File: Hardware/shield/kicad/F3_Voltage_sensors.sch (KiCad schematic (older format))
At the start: 14 parts, among them U301 LMV358, U401 LMV358

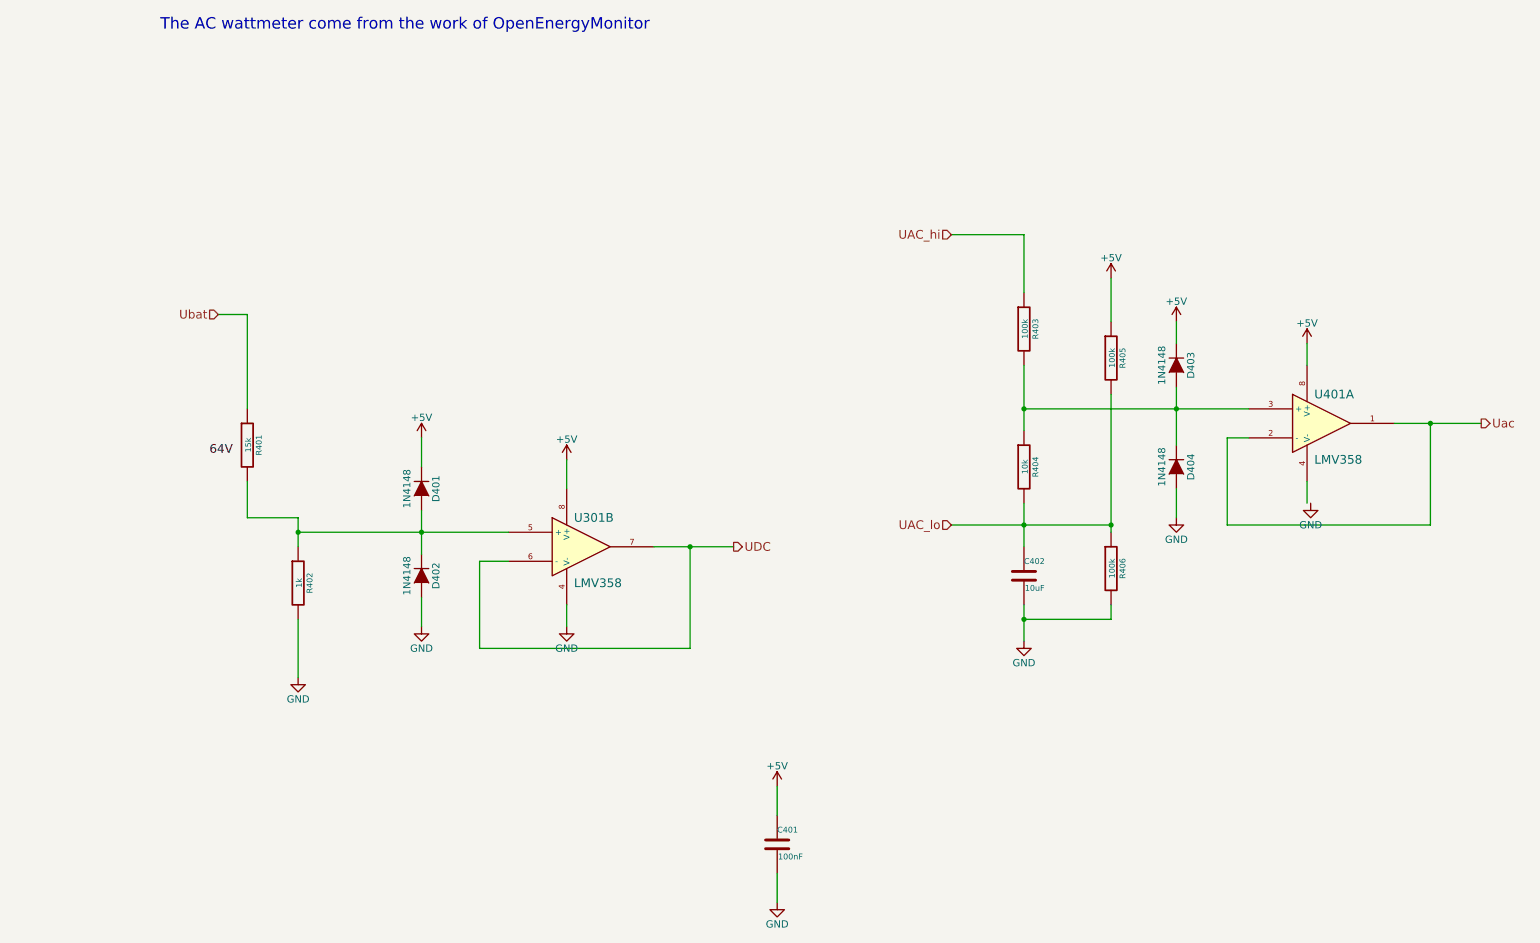
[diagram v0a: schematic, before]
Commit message: Update shield to 2.0.0
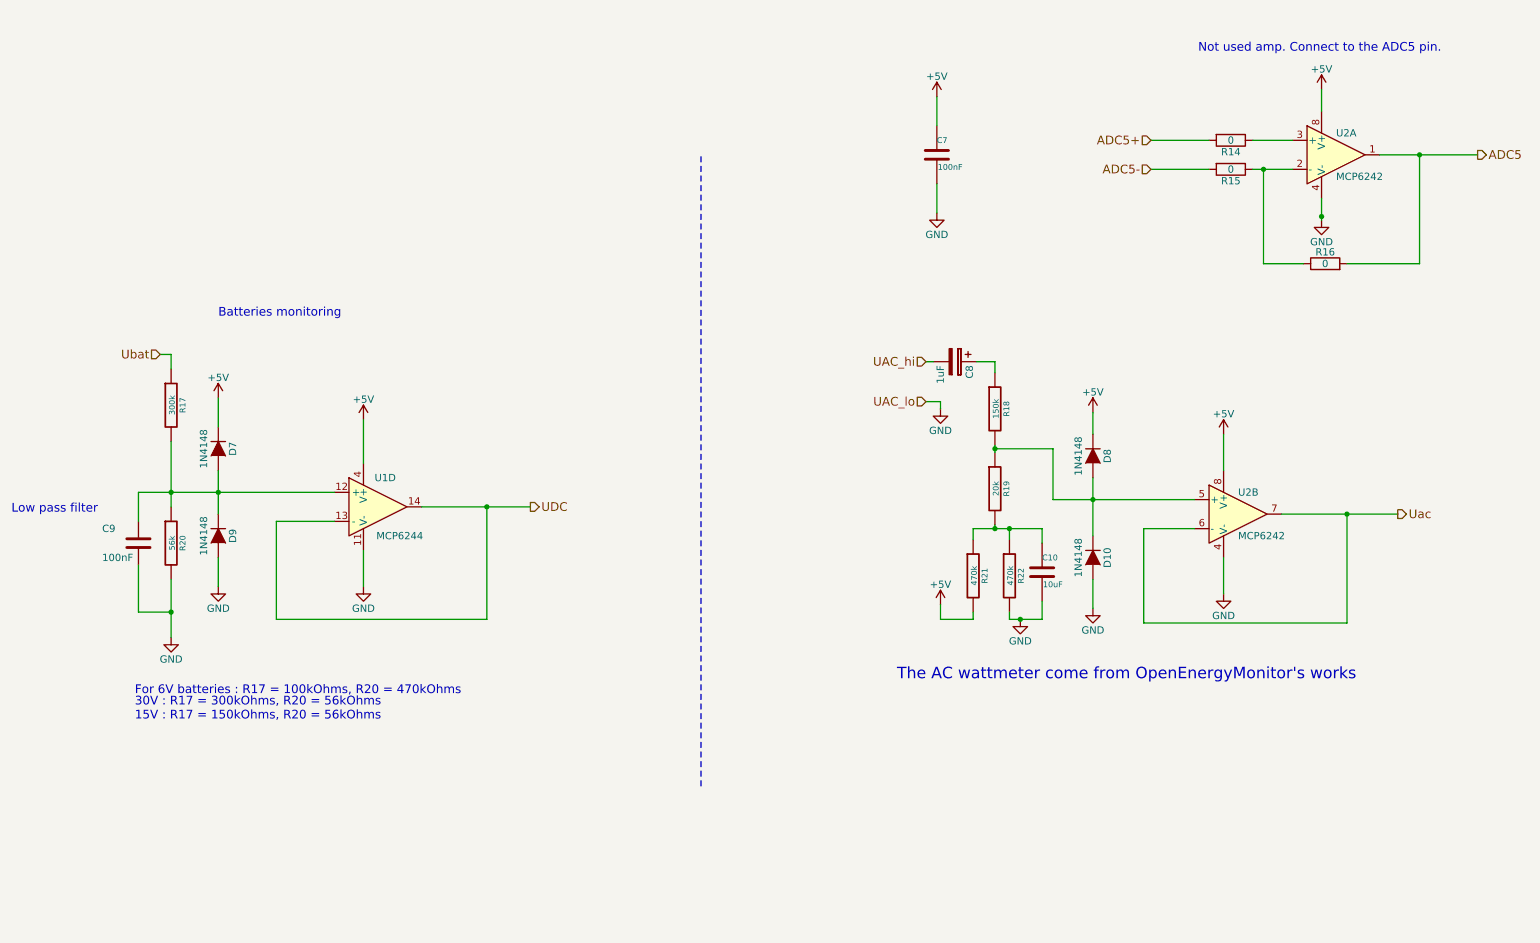
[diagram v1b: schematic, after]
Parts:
- removed U301, U401: LMV358, Housings_DIP:DIP-8_W7.62mm_LongPads, symbol LM358-RESCUE-Windlogger
- added C8: 1uF, Capacitors_ThroughHole:C_Radial_D5_L6_P2.5, symbol CP
- added C9: 100nF, Capacitors_ThroughHole:C_Rect_L7_W2.5_P5, symbol C
- added R14, R15, R16: 0, Discret:R3-LARGE_PADS, symbol R
- added U1: MCP6244, Housings_DIP:DIP-14_W7.62mm_LongPads, symbol MCP6004
- added U2: MCP6242, Housings_DIP:DIP-8_W7.62mm_LongPads, symbol MCP6002
- D10: renamed from D404; footprint Diodes_ThroughHole:Diode_DO-35_SOD27_Horizontal_RM10 -> Discret:DO-35
- D7: renamed from D401; footprint Diodes_ThroughHole:Diode_DO-35_SOD27_Horizontal_RM10 -> Discret:DO-35
- D8: renamed from D403; footprint Diodes_ThroughHole:Diode_DO-35_SOD27_Horizontal_RM10 -> Discret:DO-35
- D9: renamed from D402; footprint Diodes_ThroughHole:Diode_DO-35_SOD27_Horizontal_RM10 -> Discret:DO-35
- R17: renamed from R401; value 15k -> 300k; footprint Discret:R4 -> Discret:R3-LARGE_PADS
- R18: renamed from R403; value 100k -> 150k; footprint Discret:R4 -> Discret:R3-LARGE_PADS
- R19: renamed from R404; value 10k -> 20k; footprint Discret:R4 -> Discret:R3-LARGE_PADS
- R20: renamed from R402; value 1k -> 56k; footprint Discret:R4 -> Discret:R3-LARGE_PADS
- R21: renamed from R406; value 100k -> 470k; footprint Discret:R4 -> Discret:R3-LARGE_PADS
- R22: renamed from R405; value 100k -> 470k; footprint Discret:R4 -> Discret:R3-LARGE_PADS
- renumbered C402 to C10, C401 to C7
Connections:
- net +5V: now also R21.2, U1.4 (V+), U2.8 (V+), U2.8 (V+); no longer R22.1
- net GND: now also R22.2, C9.2, U1.11 (V-), U2.4 (V-), U2.4 (V-); no longer R21.2
- net UAC_hi: now also C8.2; no longer R18.1
- net UDC: now also U1.13 (-), U1.14
- net Uac: now also U2.6 (-), U2.7
- net at D10.1 (K), D8.2 (A), R18.2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: now also U2.5 (+)
- net at D7.2 (A), D9.1 (K), R17.2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: now also C9.1, U1.12 (+)
- net UAC_lo: no longer names the net of C10.1, R19.2, R21.1
- net UAC_lo: now also R22.1; no longer R22.2
- new net: C8.1, R18.1
- new net: R14.1, U2.3 (+)
- new net: R15.1, R16.1, U2.2 (-)
- new net ADC5: R16.2, U2.1
- new net ADC5+: R14.2
- new net ADC5-: R15.2
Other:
- note added: "30V : R17 = 300kOhms, R20 = 56kOhms\n15V : R17 = 150kOhms, R20 = 56kOhms"
- note added: "Batteries monitoring"
- note added: "For 6V batteries : R17 = 100kOhms, R20 = 470kOhms"
- note added: "Low pass filter"
- note added: "Not used amp. Connect to the ADC5 pin."
- note added: "The AC wattmeter come from OpenEnergyMonitor's works"
- note removed: "The AC wattmeter come from the work of OpenEnergyMonitor"
- moved on the sheet: C10, C7, D10, D7, D8, D9, R17, R18, R19, R20, R21, R22

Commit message: move to digital 1.1.1
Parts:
- removed C8: 1uF, Capacitors_ThroughHole:C_Radial_D5_L6_P2.5, symbol CP
- removed C9: 100nF, Capacitors_ThroughHole:C_Rect_L7_W2.5_P5, symbol C
- removed R14, R15, R16: 0, Discret:R3-LARGE_PADS, symbol R
- removed U1: MCP6244, Housings_DIP:DIP-14_W7.62mm_LongPads, symbol MCP6004
- removed U2: MCP6242, Housings_DIP:DIP-8_W7.62mm_LongPads, symbol MCP6002
- added U301, U401: LMV358, Housings_DIP:DIP-8_W7.62mm_LongPads, symbol LM358-RESCUE-Windlogger
- D401: renamed from D7; footprint Discret:DO-35 -> Diodes_ThroughHole:Diode_DO-35_SOD27_Horizontal_RM10
- D402: renamed from D9; footprint Discret:DO-35 -> Diodes_ThroughHole:Diode_DO-35_SOD27_Horizontal_RM10
- D403: renamed from D8; footprint Discret:DO-35 -> Diodes_ThroughHole:Diode_DO-35_SOD27_Horizontal_RM10
- D404: renamed from D10; footprint Discret:DO-35 -> Diodes_ThroughHole:Diode_DO-35_SOD27_Horizontal_RM10
- R401: renamed from R17; value 300k -> 15k; footprint Discret:R3-LARGE_PADS -> Discret:R4
- R402: renamed from R20; value 56k -> 1k; footprint Discret:R3-LARGE_PADS -> Discret:R4
- R403: renamed from R18; value 150k -> 100k; footprint Discret:R3-LARGE_PADS -> Discret:R4
- R404: renamed from R19; value 20k -> 10k; footprint Discret:R3-LARGE_PADS -> Discret:R4
- R405: renamed from R22; value 470k -> 100k; footprint Discret:R3-LARGE_PADS -> Discret:R4
- R406: renamed from R21; value 470k -> 100k; footprint Discret:R3-LARGE_PADS -> Discret:R4
- renumbered C7 to C401, C10 to C402
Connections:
- net +5V: now also R405.1, U301.8 (V+), U401.8 (V+); no longer R406.2
- net GND: now also R406.2, U301.4 (V-); no longer R405.2
- net UAC_hi: now also R403.1
- net UDC: now also U301.6 (-), U301.7
- net Uac: now also U401.1, U401.2 (-)
- net at D403.2 (A), D404.1 (K), R403.2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: now also U401.3 (+)
- net UAC_lo: now reaches C402.1, R404.2, R406.1
- net UAC_lo: now also R405.2; no longer R405.1
- net at D401.2 (A), D402.1 (K), R401.2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: now also U301.5 (+)
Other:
- note added: "The AC wattmeter come from the work of OpenEnergyMonitor"
- note removed: "30V : R17 = 300kOhms, R20 = 56kOhms\n15V : R17 = 150kOhms, R20 = 56kOhms"
- note removed: "Batteries monitoring"
- note removed: "For 6V batteries : R17 = 100kOhms, R20 = 470kOhms"
- note removed: "Low pass filter"
- note removed: "Not used amp. Connect to the ADC5 pin."
- note removed: "The AC wattmeter come from OpenEnergyMonitor's works"
- moved on the sheet: C401, C402, D401, D402, D403, D404, R401, R402, R403, R404, R405, R406
